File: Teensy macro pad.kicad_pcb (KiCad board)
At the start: 2 copper layers, 79 x 122.4 mm, 43 parts, among them J1 USB_C_Receptacle_USB2.0_14P, J2 AVR-ISP-6, J3 Conn_01x05_Pin, SW0,0 CherryMX, SW0,1 CherryMX, SW0,2 CherryMX, SW0,3 CherryMX, SW0,4 CherryMX, SW1 SW_Push, SW1,0 CherryMX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

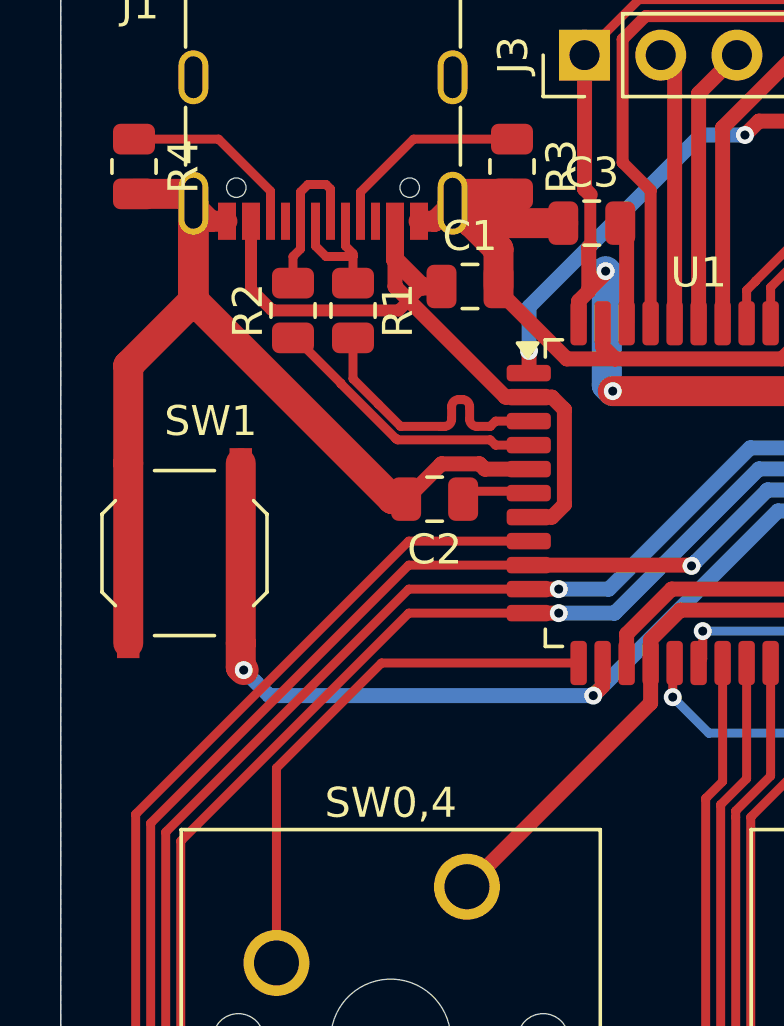
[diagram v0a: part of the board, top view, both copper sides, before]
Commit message: Move decoupling capacitors to be one per VCC pin
Pages 5 and 6 of AN2519 [0] are particularly relevant here.

[0]: https://ww1.microchip.com/downloads/aemDocuments/documents/MCU08/ApplicationNotes/ApplicationNotes/AN2519-AVR-Microcontroller-Hardware-Design-Considerations-00002519B.pdf
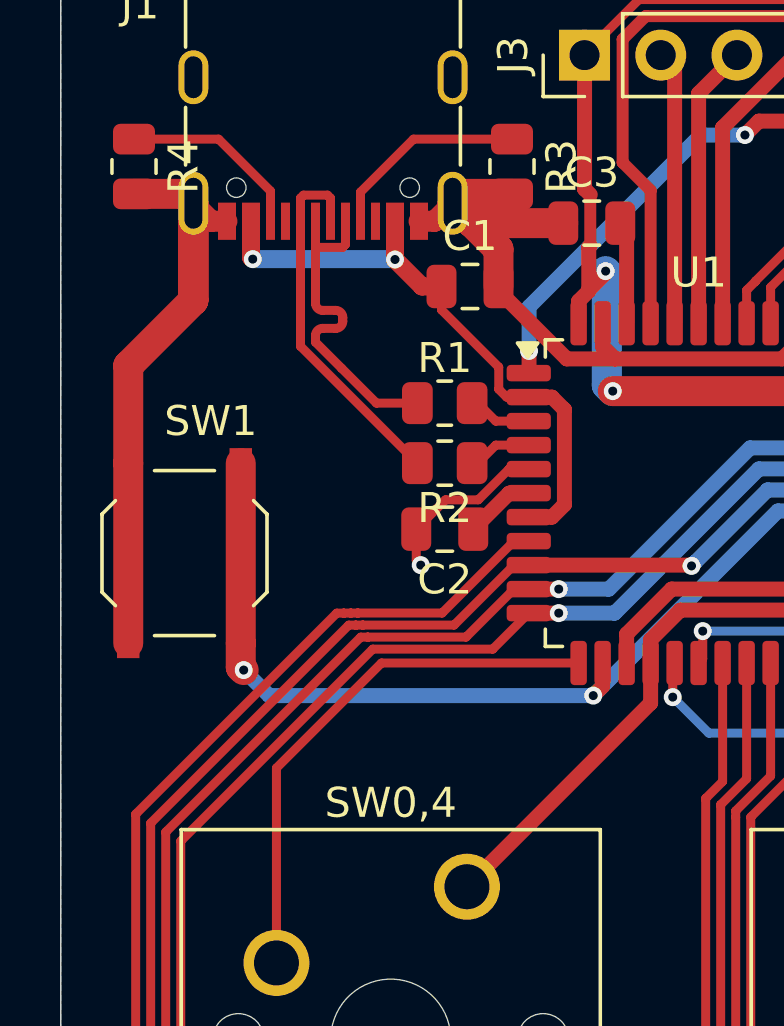
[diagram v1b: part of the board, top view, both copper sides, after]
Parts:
- moved R2 7.17 mm to (48.8, 47.8), turned to 0 degrees
- moved R1 4.35 mm to (48.8, 45.8), turned to 0 degrees
- moved C2 1.06 mm to (48.8, 50.0)
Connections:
- net Net-(J1-D+-PadA6) renamed /J1-D+
- net Net-(J1-D--PadA7) renamed /J1-D-
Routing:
- net GND: track 136.4 -> 127.8 mm, vias 0 -> 1
- net /D+: track 9.35 -> 2.14 mm
- net /D-: track 9.29 -> 2.14 mm
- net /J1-D-: track 4.39 -> 11.5 mm
- net /J1-D+: track 5.38 -> 12.3 mm
- net /VBUS: track 24.7 -> 20.6 mm, vias 0 -> 2

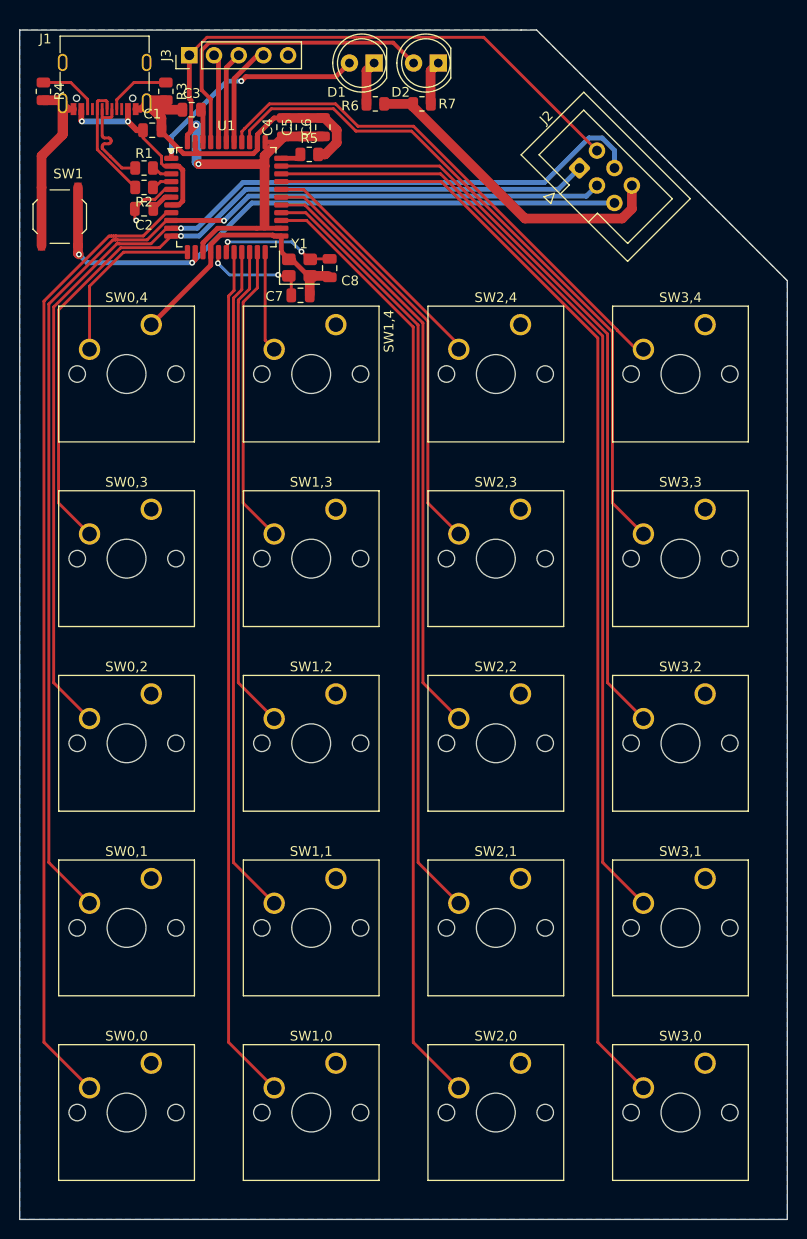
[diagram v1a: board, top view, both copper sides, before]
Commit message: Add a decoupling capacitor to VCC pin 44
This isn't on the Teensy, but AN2519 is quite clear that "For devices
with multiple pairs of power and ground pins, it is essential that there
is a decoupling capacitor for every pair of pins."
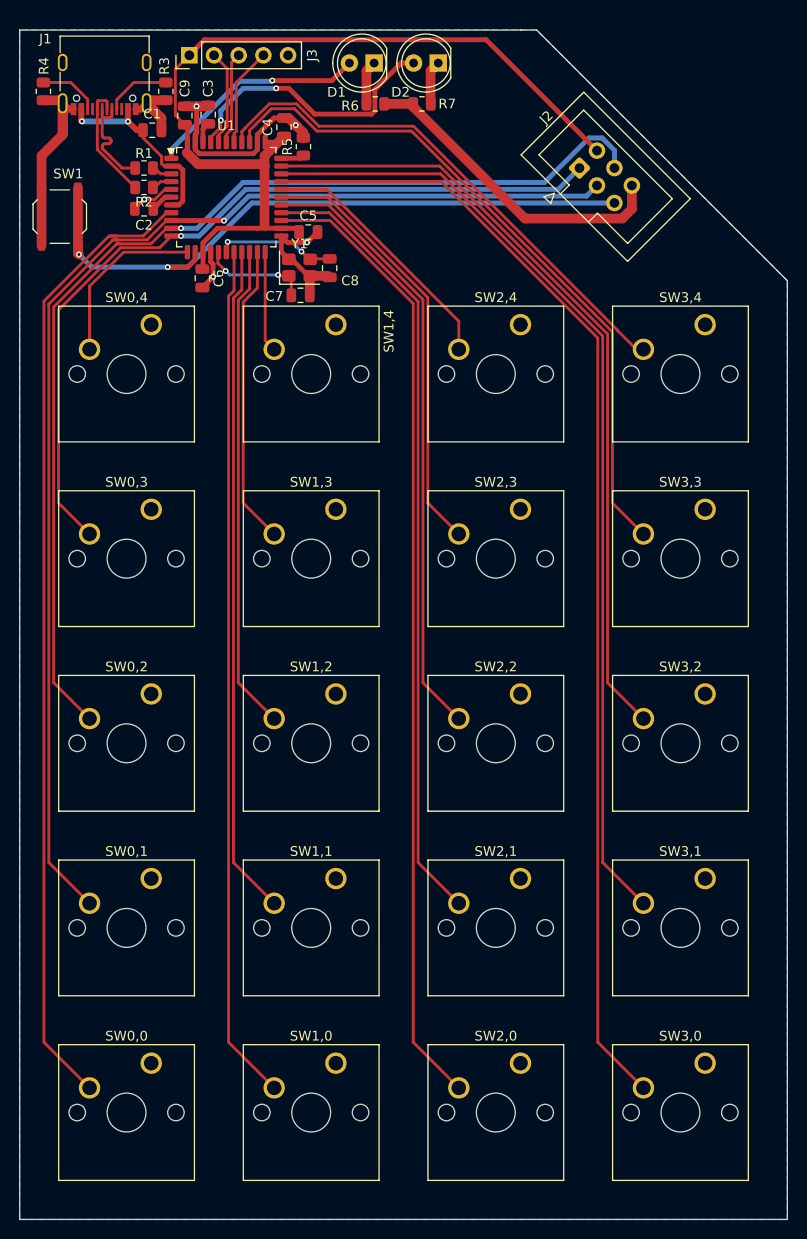
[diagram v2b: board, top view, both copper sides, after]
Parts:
- added C9: 0.1uF, Capacitor_SMD:C_0805_2012Metric, F.Cu at (53.0, 40.4)
- moved C6 19.9 mm to (54.8, 57.1), turned to -90 degrees
- moved C5 10.8 mm to (65.7, 52.4), turned to 0 degrees
- moved C3 1.77 mm to (55.4, 40.3), turned to -90 degrees
- moved R5 1.00 mm to (65.2, 43.6), turned to 90 degrees
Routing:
- net GND: track 127.8 -> 108.5 mm, vias 1 -> 5
- net Net-(D2-A): track 32.8 -> 29.0 mm, vias 0 -> 2
- net /~{RESET}: track 66.2 -> 69.2 mm
- net VCC: track 95.1 -> 92.7 mm, vias 2 -> 0
- net Net-(U1-PD4): track 98.4 -> 99.8 mm
- net Net-(U1-PB4): track 43.6 -> 45.0 mm
- net Net-(U1-PD7): track 61.8 -> 63.3 mm
- net Net-(U1-PD6): track 80.1 -> 81.5 mm
- net Net-(U1-PB5): track 25.4 -> 26.8 mm
- net Net-(U1-AREF): track 3.43 -> 2.11 mm
- net Net-(D1-A): track 23.7 -> 22.9 mm
- net Net-(J3-Pin_2): track 9.13 -> 9.87 mm

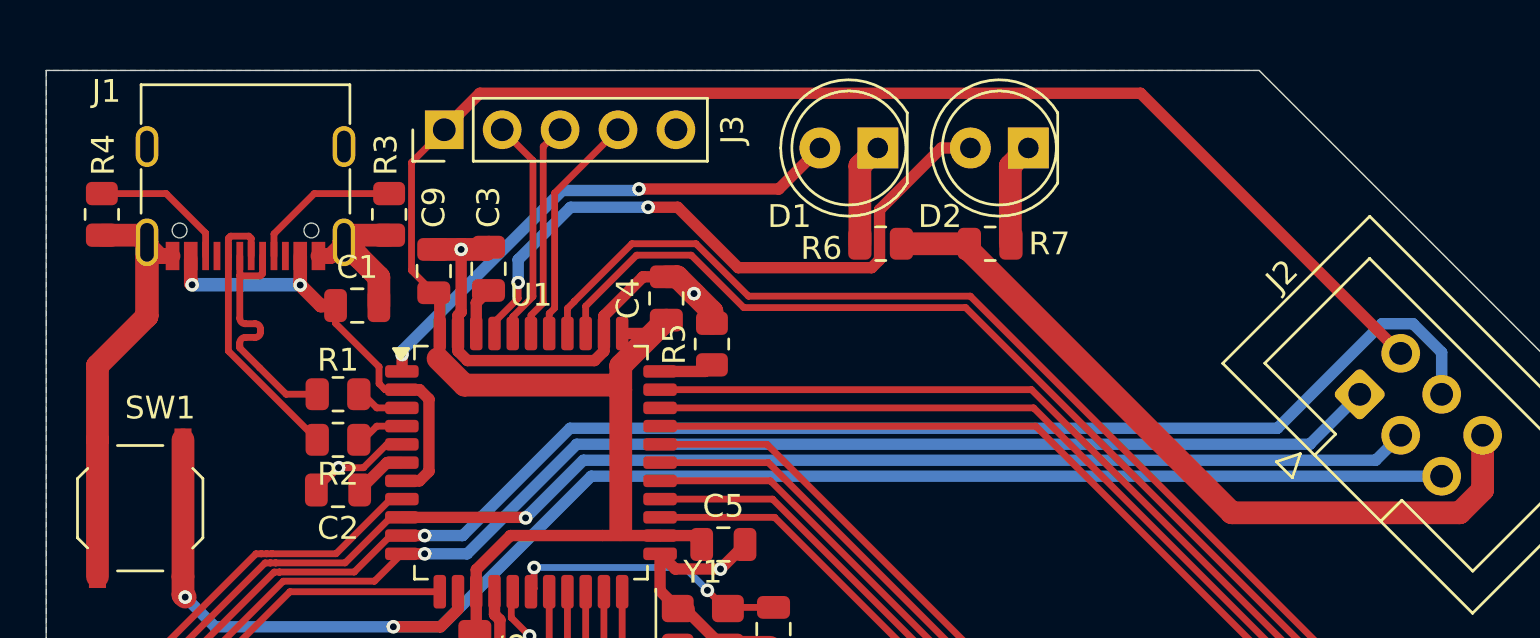
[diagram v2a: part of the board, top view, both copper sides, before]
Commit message: Change and move USB-C connector footprint
The old footprint was causing DRC errors (due to pads being too close to
its holes). Replace it with the one Matthew recommends
(...TYPE-C-31-M-12) and also move it so the edge of the connector
overhangs the board edge to make it easier to put the board in a case or
something.
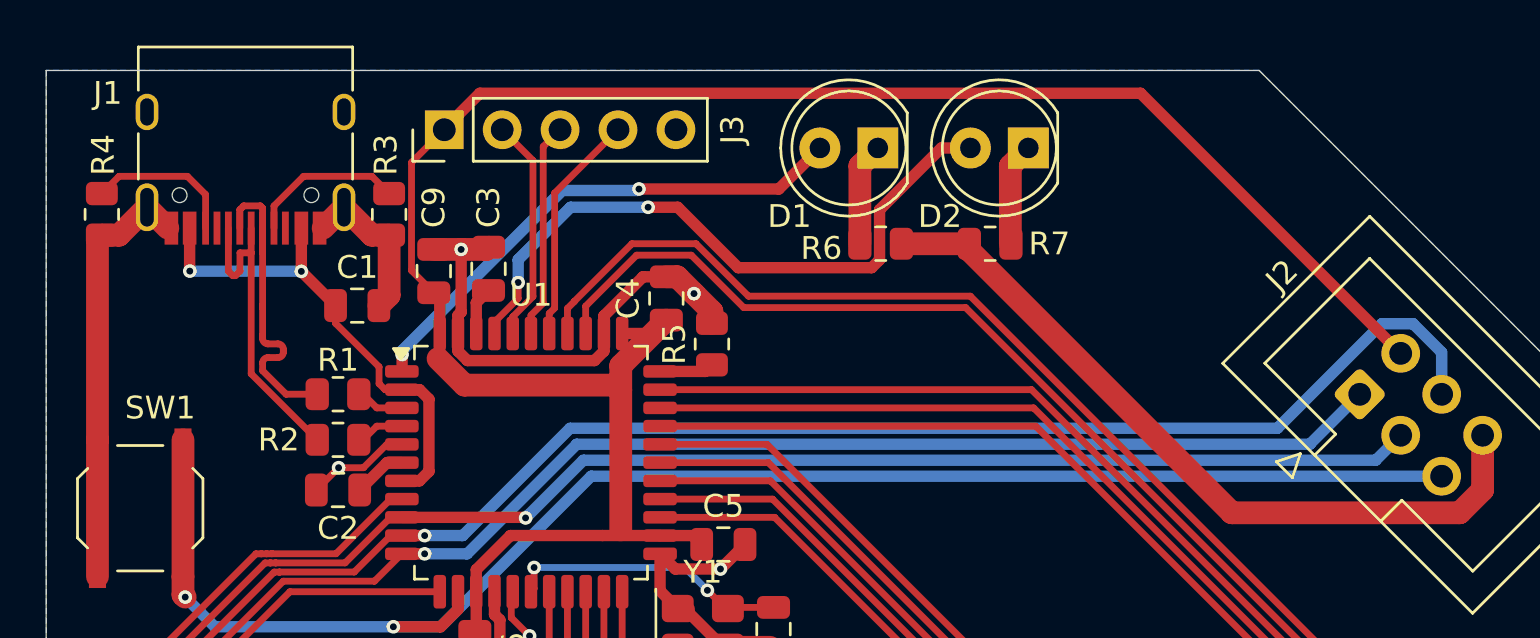
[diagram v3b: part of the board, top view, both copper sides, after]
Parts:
- J1: footprint Connector_USB:USB_C_Receptacle_G-Switch_GT-USB-7010ASV -> Connector_USB:USB_C_Receptacle_HRO_TYPE-C-31-M-12
- moved J1 1.54 mm to (44.7, 34.5)
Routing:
- net GND: track 108.5 -> 104.4 mm
- net /J1-D-: track 11.5 -> 14.3 mm
- net /J1-D+: track 12.3 -> 14.3 mm
- net /VBUS: track 20.6 -> 22.0 mm
